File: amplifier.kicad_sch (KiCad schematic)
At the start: 16 parts, among them U5 PAM8403D

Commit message: Added footprints and imported to PCB
All of them except speakers
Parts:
- C11, C12, C14, C15, C16, C17, C8, C9: footprint (none) -> Capacitor_SMD:C_0603_1608Metric
- C13: footprint (none) -> Capacitor_SMD:CP_Elec_8x10.5
- FB3, FB4: footprint (none) -> OtherComponents:FerriteBead_742861160_0603
- R7, R8: footprint (none) -> Resistor_SMD:R_0603_1608Metric
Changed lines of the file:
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@@
 			)
 		)
-		(property "Footprint" ""
+		(property "Footprint" "Capacitor_SMD:C_0603_1608Metric"
 			(at 90.17 91.7448 0)
 			(effects
@@
 			)
 		)
-		(property "Footprint" ""
+		(property "Footprint" "Capacitor_SMD:C_0603_1608Metric"
 			(at 127.9652 71.12 0)
 			(effects
@@
 			)
 		)
-		(property "Footprint" ""
+		(property "Footprint" "Capacitor_SMD:CP_Elec_8x10.5"
 			(at 147.0152 66.04 0)
 			(effects
@@
 			)
 		)
-		(property "Footprint" ""
+		(property "Footprint" "Capacitor_SMD:C_0603_1608Metric"
 			(at 96.2152 67.31 0)
 			(effects
@@
 			)
 		)
-		(property "Footprint" ""
+		(property "Footprint" "Capacitor_SMD:C_0603_1608Metric"
 			(at 166.0652 67.31 0)
 			(effects
@@
 			)
 		)
-		(property "Footprint" ""
+		(property "Footprint" "Capacitor_SMD:C_0603_1608Metric"
 			(at 119.38 86.6648 0)
 			(effects
@@
 			)
 		)
-		(property "Footprint" ""
+		(property "Footprint" "OtherComponents:FerriteBead_742861160_0603"
 			(at 156.21 80.518 90)
 			(effects
@@
 			)
 		)
-		(property "Footprint" ""
+		(property "Footprint" "Resistor_SMD:R_0603_1608Metric"
 			(at 96.52 94.488 90)
 			(effects
@@
 			)
 		)
-		(property "Footprint" ""
+		(property "Footprint" "Capacitor_SMD:C_0603_1608Metric"
 			(at 110.49 71.4248 0)
 			(effects
@@
 			)
 		)
-		(property "Footprint" ""
+		(property "Footprint" "OtherComponents:FerriteBead_742861160_0603"
 			(at 153.67 99.568 90)
 			(effects
@@
 			)
 		)
-		(property "Footprint" ""
+		(property "Footprint" "Capacitor_SMD:C_0603_1608Metric"
 			(at 162.2552 86.36 0)
 			(effects
@@
 			)
 		)
-		(property "Footprint" ""
+		(property "Footprint" "Resistor_SMD:R_0603_1608Metric"
 			(at 116.84 74.168 90)
 			(effects
@@
 			)
 		)
-		(property "Footprint" ""
+		(property "Footprint" "Capacitor_SMD:C_0603_1608Metric"
 			(at 163.5252 105.41 0)
 			(effects

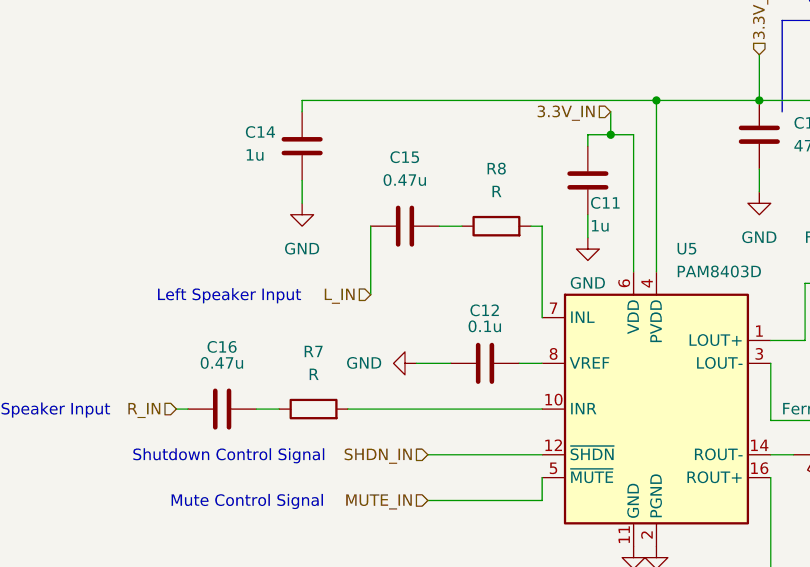
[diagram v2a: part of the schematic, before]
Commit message: Added TEMPORARY bill of materials
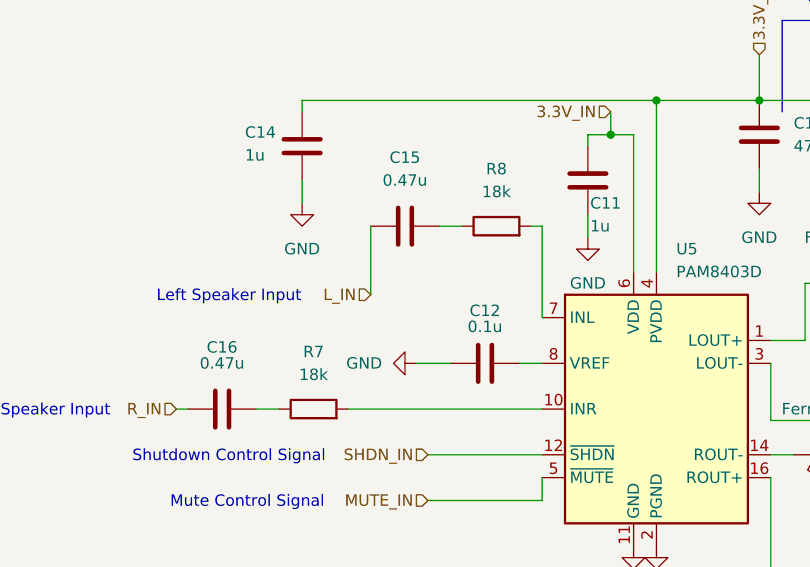
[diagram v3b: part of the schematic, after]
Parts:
- R7, R8: value R -> 18k
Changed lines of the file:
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@@
 			)
 		)
-		(property "Value" "R"
+		(property "Value" "18k"
 			(at 96.52 88.9 90)
 			(effects
@@
 			)
 		)
-		(property "Value" "R"
+		(property "Value" "18k"
 			(at 116.84 68.58 90)
 			(effects

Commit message: Added footprints for speakers
And changed size of other pin headers
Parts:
- LS1, LS2: footprint (none) -> Connector_PinHeader_1.27mm:PinHeader_1x02_P1.27mm_Vertical_SMD_Pin1Left
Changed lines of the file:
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@@
 			)
 		)
-		(property "Footprint" ""
+		(property "Footprint" "Connector_PinHeader_1.27mm:PinHeader_1x02_P1.27mm_Vertical_SMD_Pin1Left"
 			(at 189.23 110.49 0)
 			(effects
@@
 			)
 		)
-		(property "Footprint" ""
+		(property "Footprint" "Connector_PinHeader_1.27mm:PinHeader_1x02_P1.27mm_Vertical_SMD_Pin1Left"
 			(at 189.23 90.17 0)
 			(effects

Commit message: Perfection (maybe not)
:)
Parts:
- added C25, C26: 220p, Capacitor_SMD:C_0603_1608Metric, symbol Device:C
- added FB5, FB6: FerriteBead, OtherComponents:FerriteBead_742861160_0603, symbol Device:FerriteBead
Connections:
- net GND: now also C25.2, C26.2
- net at U5.16 (ROUT+): now also FB6.1; no longer LS2.2
- net at U5.3 (LOUT-): now also FB5.1; no longer LS1.2
- new net: C25.1, FB6.2, LS2.2
- new net: C26.1, FB5.2, LS1.2
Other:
- moved on the sheet: FB4
